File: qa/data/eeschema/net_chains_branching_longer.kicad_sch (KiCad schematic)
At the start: 7 parts, among them X1 OUTDRV, X2 INSINK

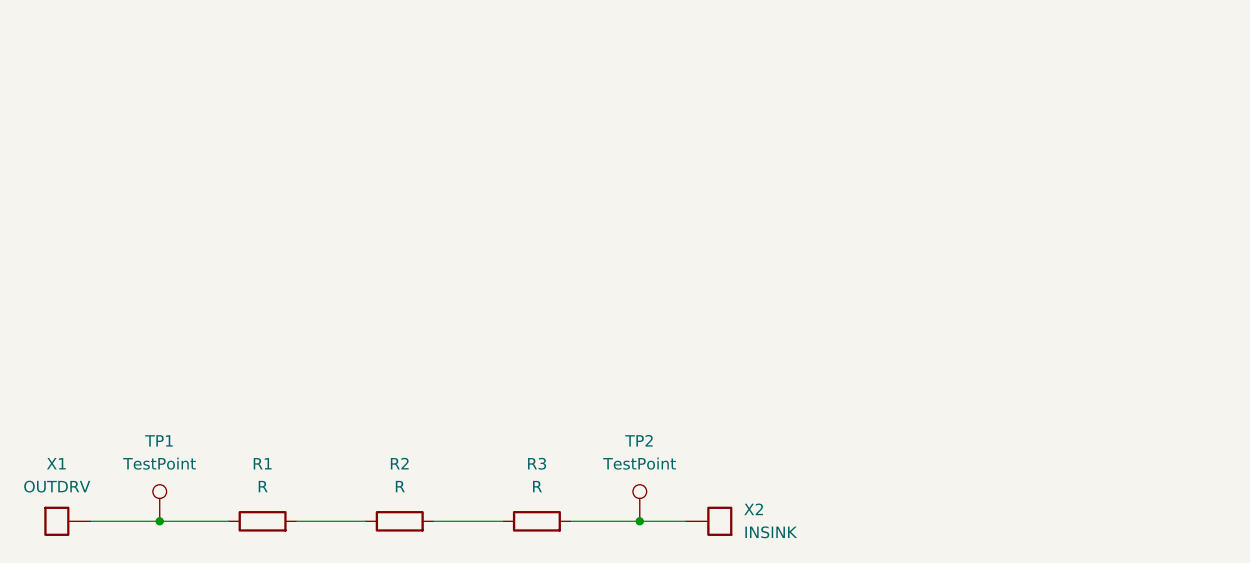
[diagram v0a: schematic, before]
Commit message: Fully rename signals to netchain
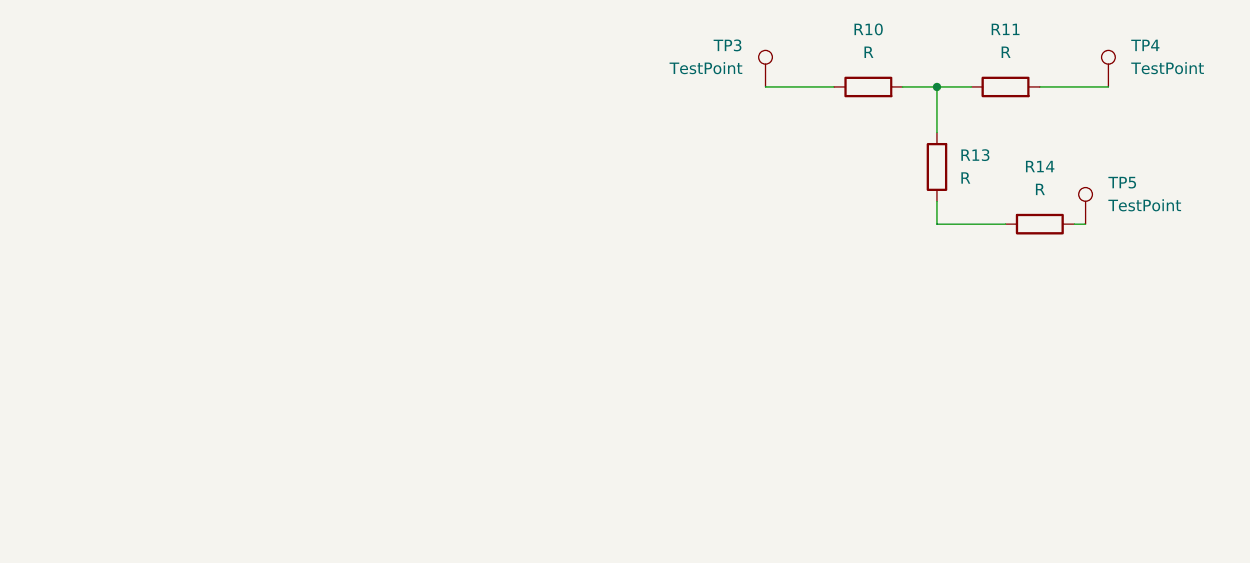
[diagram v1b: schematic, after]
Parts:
- removed R1, R2, R3: R, symbol Device:R
- removed TP1, TP2: TestPoint, symbol Connector:TestPoint
- removed X1: OUTDRV, symbol Custom:OUTDRV
- removed X2: INSINK, symbol Custom:OUTDRV
- added R10, R11, R13, R14: R, Resistor_SMD:R_0603_1608Metric, symbol Device:R
- added TP3, TP4, TP5: TestPoint, MountingHole:MountingHole_2.2mm_M2_DIN965_Pad, symbol Connector:TestPoint
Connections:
- new net: R10.1, TP3.1
- new net: R13.1, R14.2
- new net: R10.2, R11.1, R13.2
- new net: R11.2, TP4.1
- new net: R14.1, TP5.1
